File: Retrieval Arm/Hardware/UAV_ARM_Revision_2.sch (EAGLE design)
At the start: 19 parts, among them Q1 Q_ATMEGA328P, Q2 Q_LTC490, Q3 Q_LDO

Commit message: Cleaned up the schematic. I used ports to make the schematic easier to read. I rerouted some traces, but it looks about the same on the board side. I also added a capacitor.
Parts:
- added C3: 0.1uF, SparkFun-Capacitors:CAP1206
- C1: value 1uF -> 0.1uF
- C4: value .1uF -> 0.1uF
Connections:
- net N$12 renamed PC2
- net N$13 renamed PC1
- net N$16 renamed PC5
- net N$17 renamed PD5
- net N$18 renamed 5V
- net N$19 renamed PC4
- net N$20 renamed PC3
- net N$21 renamed PB1
- net N$22 renamed PD3
- net N$6 renamed PC0
- net N$7 renamed TX_1
- net N$8 renamed RX_1
- removed net N$5 (its old number): D1.C, JP1.2, Q3.VIN
- new net VIN: C3.1, D1.C, JP1.2, Q3.VIN
- net GND: now also C3.2
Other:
- moved on the sheet: C1, C2, C4, C6, C7, D1, JP3, Q2, Q3, R1, R2, U$1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

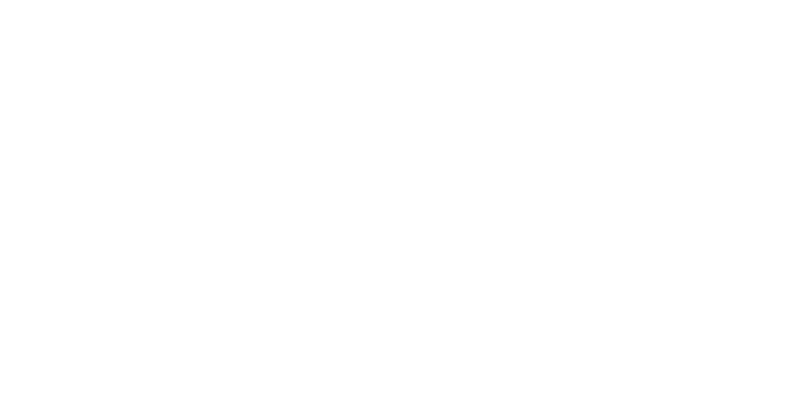
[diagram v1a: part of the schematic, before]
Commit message: Added grounded mounting holes
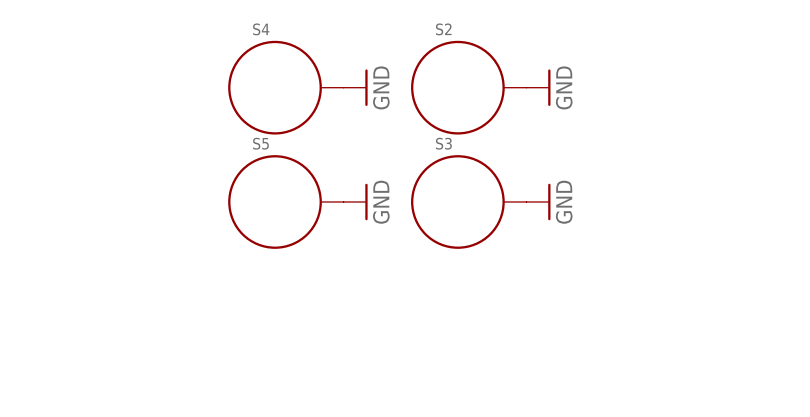
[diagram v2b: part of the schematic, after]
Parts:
- added S2, S3, S4, S5: STANDOFF_ELECTRICAL, SparkFun-Electromechanical:STANDOFF_ELECTRICAL
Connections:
- net GND: now also S2.P$1, S3.P$1, S4.P$1, S5.P$1
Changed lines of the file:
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@@
 <part name="GND8" library="SparkFun-Aesthetics" deviceset="GND" device=""/>
 <part name="GND9" library="SparkFun-Aesthetics" deviceset="GND" device=""/>
+<part name="S2" library="SparkFun-Electromechanical" deviceset="STANDOFF_ELECTRICAL" device=""/>
+<part name="S3" library="SparkFun-Electromechanical" deviceset="STANDOFF_ELECTRICAL" device=""/>
+<part name="S4" library="SparkFun-Electromechanical" deviceset="STANDOFF_ELECTRICAL" device=""/>
+<part name="S5" library="SparkFun-Electromechanical" deviceset="STANDOFF_ELECTRICAL" device=""/>
+<part name="GND5" library="SparkFun-Aesthetics" deviceset="GND" device=""/>
+<part name="GND10" library="SparkFun-Aesthetics" deviceset="GND" device=""/>
+<part name="GND11" library="SparkFun-Aesthetics" deviceset="GND" device=""/>
+<part name="GND12" library="SparkFun-Aesthetics" deviceset="GND" device=""/>
 </parts>
 <sheets>
@@
 <instance part="GND8" gate="1" x="111.76" y="33.02"/>
 <instance part="GND9" gate="1" x="137.16" y="48.26"/>
+<instance part="S2" gate="G$1" x="127" y="114.3"/>
+<instance part="S3" gate="G$1" x="127" y="101.6"/>
+<instance part="S4" gate="G$1" x="106.68" y="114.3"/>
+<instance part="S5" gate="G$1" x="106.68" y="101.6"/>
+<instance part="GND5" gate="1" x="116.84" y="114.3" rot="R90"/>
+<instance part="GND10" gate="1" x="116.84" y="101.6" rot="R90"/>
+<instance part="GND11" gate="1" x="137.16" y="114.3" rot="R90"/>
+<instance part="GND12" gate="1" x="137.16" y="101.6" rot="R90"/>
 </instances>
 <busses>
@@
 <wire x1="137.16" y1="15.24" x2="137.16" y2="12.7" width="0.1524" layer="91"/>
 </segment>
-</net>
+<segment>
+<pinref part="S4" gate="G$1" pin="P$1"/>
+<pinref part="GND5" gate="1" pin="GND"/>
+</segment>
+<segment>
+<pinref part="S5" gate="G$1" pin="P$1"/>
+<pinref part="GND10" gate="1" pin="GND"/>
+</segment>
+<segment>
+<pinref part="S2" gate="G$1" pin="P$1"/>
+<pinref part="GND11" gate="1" pin="GND"/>
+</segment>
+<segment>
+<pinref part="S3" gate="G$1" pin="P$1"/>
+<pinref part="GND12" gate="1" pin="GND"/>
+</segment>
+</net>

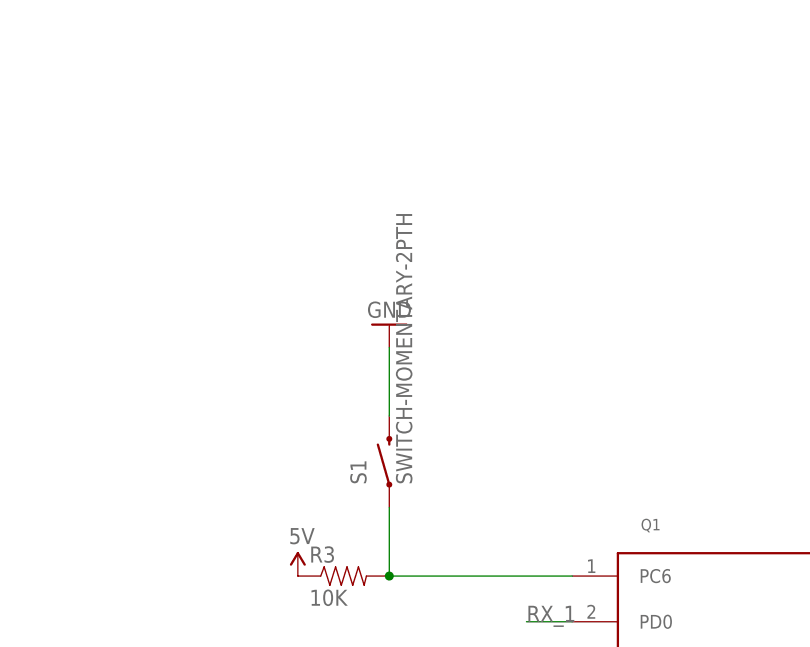
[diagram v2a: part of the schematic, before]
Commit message: Reduce Board Size and Add Surface Mount Components.
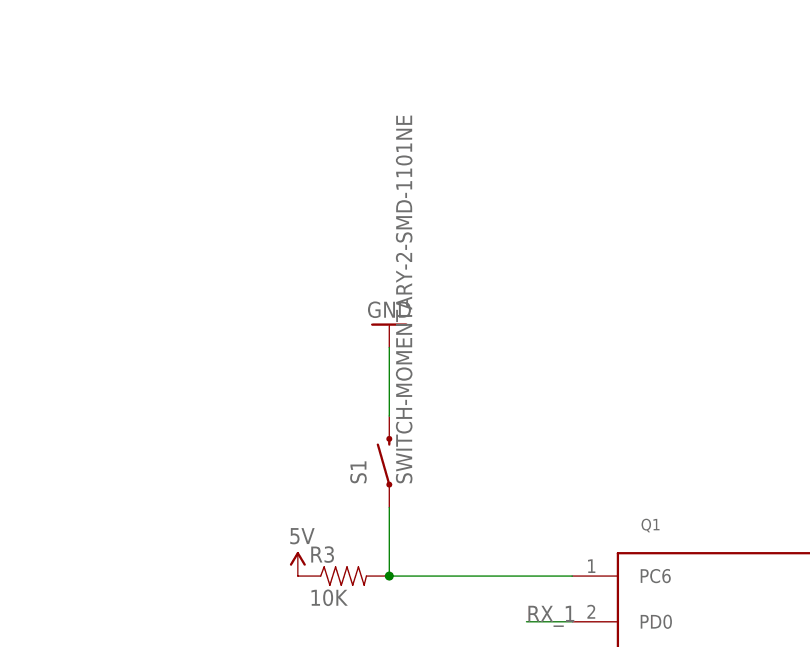
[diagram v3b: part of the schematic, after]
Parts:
- S1: value SWITCH-MOMENTARY-2PTH -> SWITCH-MOMENTARY-2-SMD-1101NE; device SparkFun-Electromechanical:SWITCH-MOMENTARY-2PTH -> SparkFun-Electromechanical:SWITCH-MOMENTARY-2-SMD-1101NE
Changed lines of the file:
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@@
 <?xml version="1.0" encoding="utf-8"?>
 <!DOCTYPE eagle SYSTEM "eagle.dtd">
-<eagle version="6.5.0">
+<eagle version="7.1.0">
 <drawing>
 <settings>
@@
 <layer number="140" name="Page" color="7" fill="1" visible="yes" active="yes"/>
 <layer number="141" name="Fabrication" color="7" fill="1" visible="yes" active="yes"/>
+<layer number="142" name="AMD" color="7" fill="1" visible="yes" active="yes"/>
+<layer number="143" name="PMD" color="7" fill="1" visible="yes" active="yes"/>
 <layer number="144" name="Drill Legend" color="7" fill="1" visible="yes" active="yes"/>
 <layer number="150" name="Notes" color="7" fill="1" visible="yes" active="yes"/>
@@
 <part name="GND4" library="supply1" deviceset="GND" device=""/>
 <part name="JP3" library="SparkFun-Connectors" deviceset="M02" device="3.5MM"/>
-<part name="S1" library="SparkFun-Electromechanical" deviceset="SWITCH-MOMENTARY-2" device="PTH"/>
+<part name="S1" library="SparkFun-Electromechanical" deviceset="SWITCH-MOMENTARY-2" device="-SMD-1101NE" value="SWITCH-MOMENTARY-2-SMD-1101NE"/>
 <part name="JP1" library="SparkFun-Connectors" deviceset="M03" device="POLAR"/>
 <part name="C2" library="SparkFun-Passives" deviceset="CAP" device="1206" value="1uF"/>

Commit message: Replace actuators with motor controller
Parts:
- removed JP3: M023.5MM, SparkFun-Connectors:M023.5MM
- removed JP7, JP8: (no value), SparkFun-Connectors:M06POLAR
- added C5: 0.1uF, SparkFun-Passives:CAP1206
- added R4, R5, R6, R7: 4.7k, SparkFun-Passives:RESISTOR1206
- added R8: 1K, SparkFun-Passives:RESISTOR1206
- added U$2: BTM7752G, MRDT-2015-General:BTM7752G
- added U$3: 100UF-ELECTRO-CAP, New:100UF-ELECTRO-CAP
- added U$4, U$5: H_WR-TBL_3210002VERT, MRDT-2015-PowerBoard:H_WR-TBL_3210002VERT
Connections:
- removed net PC0: JP8.3, Q1.PC0
- removed net PC1: JP8.2, Q1.PC1
- removed net PC2: JP8.1, Q1.PC2
- removed net PC3: JP7.3, Q1.PC3
- removed net PC4: JP7.2, Q1.PC4
- removed net PC5: JP7.1, Q1.PC5
- removed net PD3: JP7.4, Q1.PD3
- removed net PD5: JP8.4, Q1.PD5
- new net IN1: Q1.PB3, R4.1
- new net IN2: Q1.PB2, R5.1
- new net IS: Q1.PB4, R7.1
- new net N$12: R6.1, U$2.INH
- new net N$17: C5.2, U$2.VS, U$3.POS
- new net N$6: R5.2, U$2.IN2
- new net N$7: R4.2, U$2.IN1
- new net N$8: R7.2, R8.2, U$2.IS
- new net NH: Q1.PB5, R6.2
- new net OUT1: U$2.OUT1, U$5.L
- new net OUT2: U$2.OUT2, U$5.R
- net 5V: no longer JP7.5, JP8.5
- net GND: now also C5.1, R8.1, U$2.GND, U$3.NEG, U$4.R; no longer JP3.1, JP7.6, JP8.6
- net N$5: now also U$4.L; no longer JP3.2
